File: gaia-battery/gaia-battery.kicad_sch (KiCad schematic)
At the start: 3 parts, among them J1 Conn_02x10_Odd_Even, J2 Conn_02x10_Odd_Even, J3 Conn_01x02_Pin

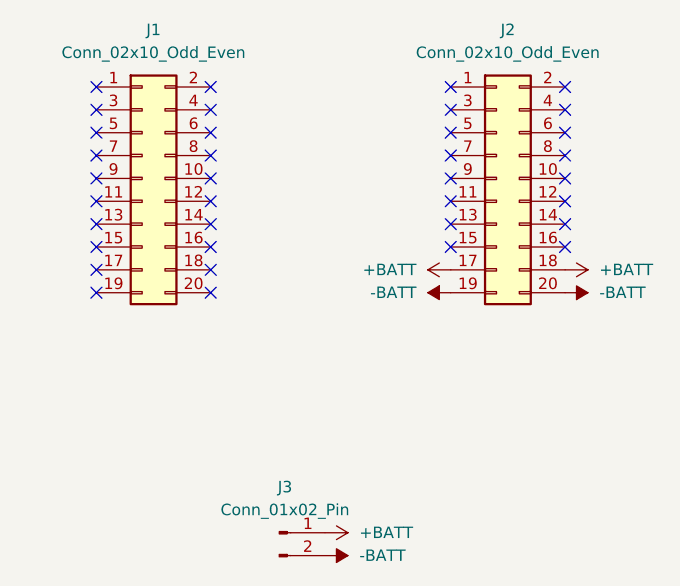
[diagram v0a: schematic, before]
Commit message: fixing routing problems
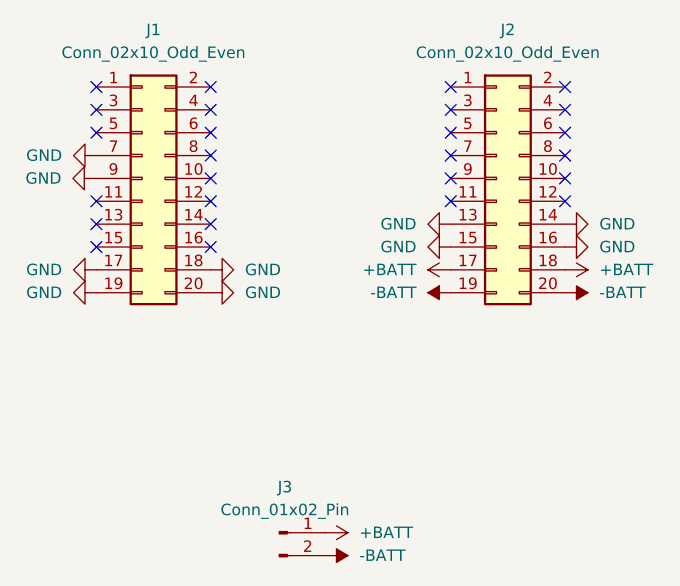
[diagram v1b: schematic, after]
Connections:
- net GND: now reaches J2.13 (Pin_13)
- net GND: now also J1.17 (Pin_17), J1.18 (Pin_18), J1.19 (Pin_19), J1.20 (Pin_20), J1.7 (Pin_7), J2.14 (Pin_14), J2.15 (Pin_15), J2.16 (Pin_16)
- no-connect marks 36 -> 26

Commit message: v1.1 - adding rtc battery
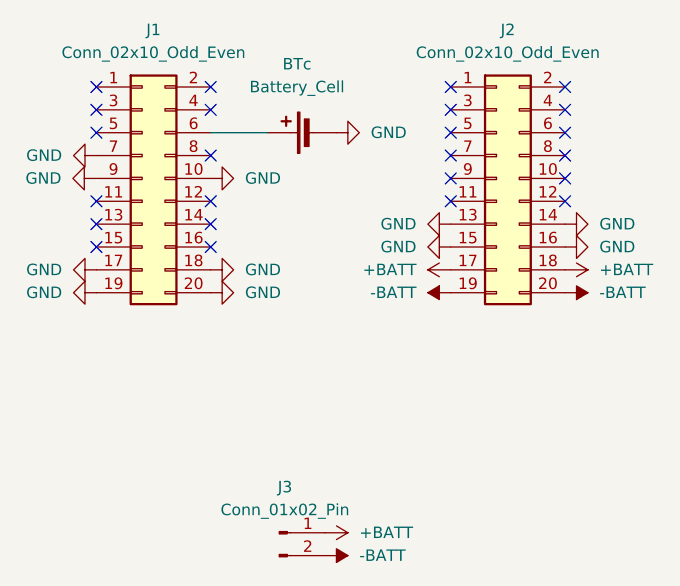
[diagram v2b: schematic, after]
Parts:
- added BTc: Battery_Cell, gaia-battery:BAT-SMD_MY-1220-03, symbol Device:Battery_Cell
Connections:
- net GND: now also J1.10 (Pin_10), BTc.2 (-)
- net at J1.6 (Pin_6): now also BTc.1 (+)
- no-connect marks 26 -> 24
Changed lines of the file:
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@@
-	)
-	(no_connect
-		(at 85.09 101.6)
 	)
 	(no_connect
@@
 	)
 	(no_connect
-		(at 85.09 96.52)
-	)
-	(no_connect
 		(at 111.76 104.14)
 	)
@@
 	(no_connect
 		(at 85.09 99.06)
+	)
+	(wire
+		(pts
+			(xy 91.44 96.52) (xy 85.09 96.52)
+		)
+		(stroke
+			(width 0)
+			(type default)
+		)
 	)
 	(symbol
@@
 	)
 	(symbol
+		(lib_id "Device:Battery_Cell")
+		(at 96.52 96.52 90)
+		(unit 1)
+		(exclude_from_sim no)
+		(in_bom yes)
+		(on_board yes)
+		(dnp no)
+		(fields_autoplaced yes)
+		(property "Reference" "BTc"
+			(at 94.6785 88.9 90)
+			(effects
+				(font
+					(size 1.27 1.27)
+				)
+			)
+		)
+		(property "Value" "Battery_Cell"
+			(at 94.6785 91.44 90)
+			(effects
+				(font
+					(size 1.27 1.27)
+				)
+			)
+		)
+		(property "Footprint" "gaia-battery:BAT-SMD_MY-1220-03"
+			(at 94.996 96.52 90)
+			(effects
+				(font
+					(size 1.27 1.27)
+				)
+				(hide yes)
+			)
+		)
+		(property "Datasheet" "~"
+			(at 94.996 96.52 90)
+			(effects
+				(font
+					(size 1.27 1.27)
+				)
+				(hide yes)
+			)
+		)
+		(property "Description" "Single-cell battery"
+			(at 96.52 96.52 0)
+			(effects
+				(font
+					(size 1.27 1.27)
+				)
+				(hide yes)
+			)
+		)
+		(pin "1"
+		)
+		(pin "2"
+		)
+		(instances
+			(project ""
+				(path "/def68c8a-9d0a-421b-b57f-431e13992b76"
+					(reference "BTc")
+					(unit 1)
+				)
+			)
+		)
+	)
+	(symbol
 		(lib_id "power:-BATT")
 		(at 111.76 114.3 90)
@@
 	(symbol
 		(lib_id "power:GND")
+		(at 85.09 101.6 90)
+		(unit 1)
+		(exclude_from_sim no)
+		(in_bom yes)
+		(on_board yes)
+		(dnp no)
+		(fields_autoplaced yes)
+		(property "Reference" "#PWR0190"
+			(at 91.44 101.6 0)
+			(effects
+				(font
+					(size 1.27 1.27)
+				)
+				(hide yes)
+			)
+		)
+		(property "Value" "GND"
+			(at 88.9 101.5999 90)
+			(effects
+				(font
+					(size 1.27 1.27)
+				)
+				(justify right)
+			)
+		)
+		(property "Footprint" ""
+			(at 85.09 101.6 0)
+			(effects
+				(font
+					(size 1.27 1.27)
+				)
+				(hide yes)
+			)
+		)
+		(property "Datasheet" ""
+			(at 85.09 101.6 0)
+			(effects
+				(font
+					(size 1.27 1.27)
+				)
+				(hide yes)
+			)
+		)
+		(property "Description" "Power symbol creates a global label with name \"GND\" , ground"
+			(at 85.09 101.6 0)
+			(effects
+				(font
+					(size 1.27 1.27)
+				)
+				(hide yes)
+			)
+		)
+		(pin "1"
+		)
+		(instances
+			(project "gaia-battery"
+				(path "/def68c8a-9d0a-421b-b57f-431e13992b76"
+					(reference "#PWR0190")
+					(unit 1)
+				)
+			)
+		)
+	)
+	(symbol
+		(lib_id "power:GND")
 		(at 72.39 114.3 270)
 		(unit 1)
@@
 					(unit 1)
 				)
+			)
+		)
+	)
+	(symbol
+		(lib_id "power:GND")
+		(at 99.06 96.52 90)
+		(unit 1)
+		(exclude_from_sim no)
+		(in_bom yes)
+		(on_board yes)
+		(dnp no)
+		(fields_autoplaced yes)
+		(property "Reference" "#PWR013"
+			(at 105.41 96.52 0)
+			(effects
+				(font
+					(size 1.27 1.27)
+				)
+				(hide yes)
+			)
+		)
+		(property "Value" "GND"
+			(at 102.87 96.5199 90)
+			(effects
+				(font
+					(size 1.27 1.27)
+				)
+				(justify right)
+			)
+		)
+		(property "Footprint" ""
+			(at 99.06 96.52 0)
+			(effects
+				(font
+					(size 1.27 1.27)
+				)
+				(hide yes)
+			)
+		)
+		(property "Datasheet" ""
+			(at 99.06 96.52 0)
+			(effects
+				(font
+					(size 1.27 1.27)
+				)
+				(hide yes)
+			)
+		)
+		(property "Description" "Power symbol creates a global label with name \"GND\" , ground"
+			(at 99.06 96.52 0)
+			(effects
+				(font
+					(size 1.27 1.27)
+				)
+				(hide yes)
+			)
+		)
+		(pin "1"
+		)
+		(instances
+			(project "gaia-battery"
+				(path "/def68c8a-9d0a-421b-b57f-431e13992b76"
+					(reference "#PWR013")
+					(unit 1)
+				)

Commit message: v1.1 gnd fix
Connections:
- net GND: now also J1.5 (Pin_5), J1.9 (Pin_9)
- no-connect marks 24 -> 23
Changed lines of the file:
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@@
-	)
-	(no_connect
-		(at 72.39 96.52)
 	)
 	(no_connect
@@
 	(symbol
 		(lib_id "power:GND")
+		(at 72.39 96.52 270)
+		(unit 1)
+		(exclude_from_sim no)
+		(in_bom yes)
+		(on_board yes)
+		(dnp no)
+		(fields_autoplaced yes)
+		(property "Reference" "#PWR014"
+			(at 66.04 96.52 0)
+			(effects
+				(font
+					(size 1.27 1.27)
+				)
+				(hide yes)
+			)
+		)
+		(property "Value" "GND"
+			(at 68.58 96.5199 90)
+			(effects
+				(font
+					(size 1.27 1.27)
+				)
+				(justify right)
+			)
+		)
+		(property "Footprint" ""
+			(at 72.39 96.52 0)
+			(effects
+				(font
+					(size 1.27 1.27)
+				)
+				(hide yes)
+			)
+		)
+		(property "Datasheet" ""
+			(at 72.39 96.52 0)
+			(effects
+				(font
+					(size 1.27 1.27)
+				)
+				(hide yes)
+			)
+		)
+		(property "Description" "Power symbol creates a global label with name \"GND\" , ground"
+			(at 72.39 96.52 0)
+			(effects
+				(font
+					(size 1.27 1.27)
+				)
+				(hide yes)
+			)
+		)
+		(pin "1"
+		)
+		(instances
+			(project "gaia-battery"
+				(path "/def68c8a-9d0a-421b-b57f-431e13992b76"
+					(reference "#PWR014")
+					(unit 1)
+				)
+			)
+		)
+	)
+	(symbol
+		(lib_id "power:GND")
 		(at 85.09 111.76 90)
 		(unit 1)
@@
 	(symbol
 		(lib_id "power:GND")
-		(at 72.3118 101.6 270)
+		(at 72.39 101.6 270)
 		(unit 1)
 		(exclude_from_sim no)
@@
 		(fields_autoplaced yes)
 		(property "Reference" "#PWR011"
-			(at 65.9618 101.6 0)
+			(at 66.04 101.6 0)
 			(effects
 				(font
@@
 		)
 		(property "Value" "GND"
-			(at 68.5018 101.5999 90)
+			(at 68.58 101.5999 90)
 			(effects
 				(font
@@
 		)
 		(property "Footprint" ""
-			(at 72.3118 101.6 0)
+			(at 72.39 101.6 0)
 			(effects
 				(font
@@
 		)
 		(property "Datasheet" ""
-			(at 72.3118 101.6 0)
+			(at 72.39 101.6 0)
 			(effects
 				(font
@@
 		)
 		(property "Description" "Power symbol creates a global label with name \"GND\" , ground"
-			(at 72.3118 101.6 0)
-			(effects
-				(font
+			(at 72.39 101.6 0)
+			(effects
+				(font

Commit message: Update gaia-battery.kicad_sch
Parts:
- renumbered BTc to BTc1
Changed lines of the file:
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@@
 		(dnp no)
 		(fields_autoplaced yes)
-		(property "Reference" "BTc"
+		(property "Reference" "BTc1"
 			(at 94.6785 88.9 90)
 			(effects
@@
 			(project ""
 				(path "/def68c8a-9d0a-421b-b57f-431e13992b76"
-					(reference "BTc")
+					(reference "BTc1")
 					(unit 1)
 				)
